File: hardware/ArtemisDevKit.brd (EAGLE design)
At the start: 94 x 38.1 mm, 228 parts, among them J2 CORTEX_JTAG_DEBUG_MINIMUM_PTH, J3 CORTEX_JTAG_DEBUG_PTH, J5 1X04_SMD_STRAIGHT_COMBO, J6 QWIIC_RIGHT_ANGLE, J7 CAMERA-HIMAX, J9 1X04_SMD_STRAIGHT_COMBO, U1 DAPLINK_KL26Z, U2 ARTEMIS_MODULESMD, U3 LIS2DH12, U4 AP2127K-1.8V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

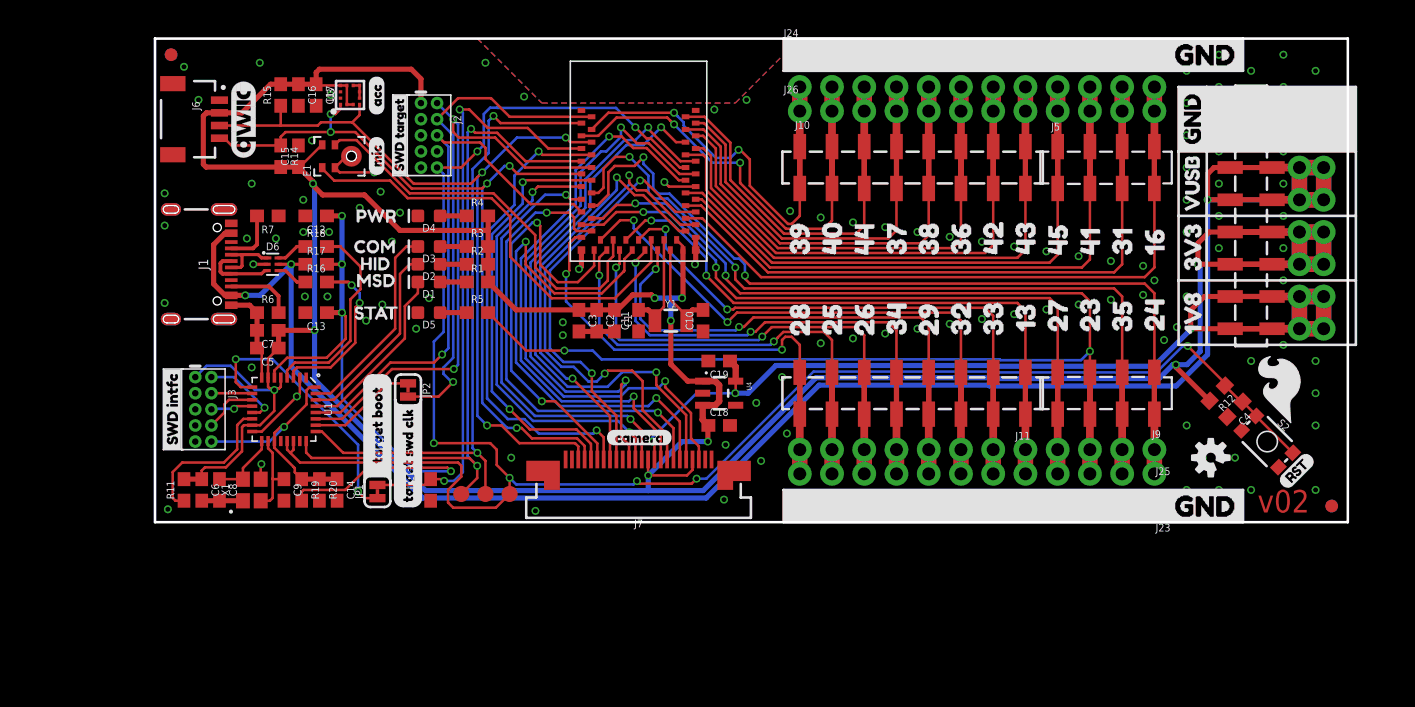
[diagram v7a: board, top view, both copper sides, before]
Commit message: remove old buzzard libraries and delete old silk
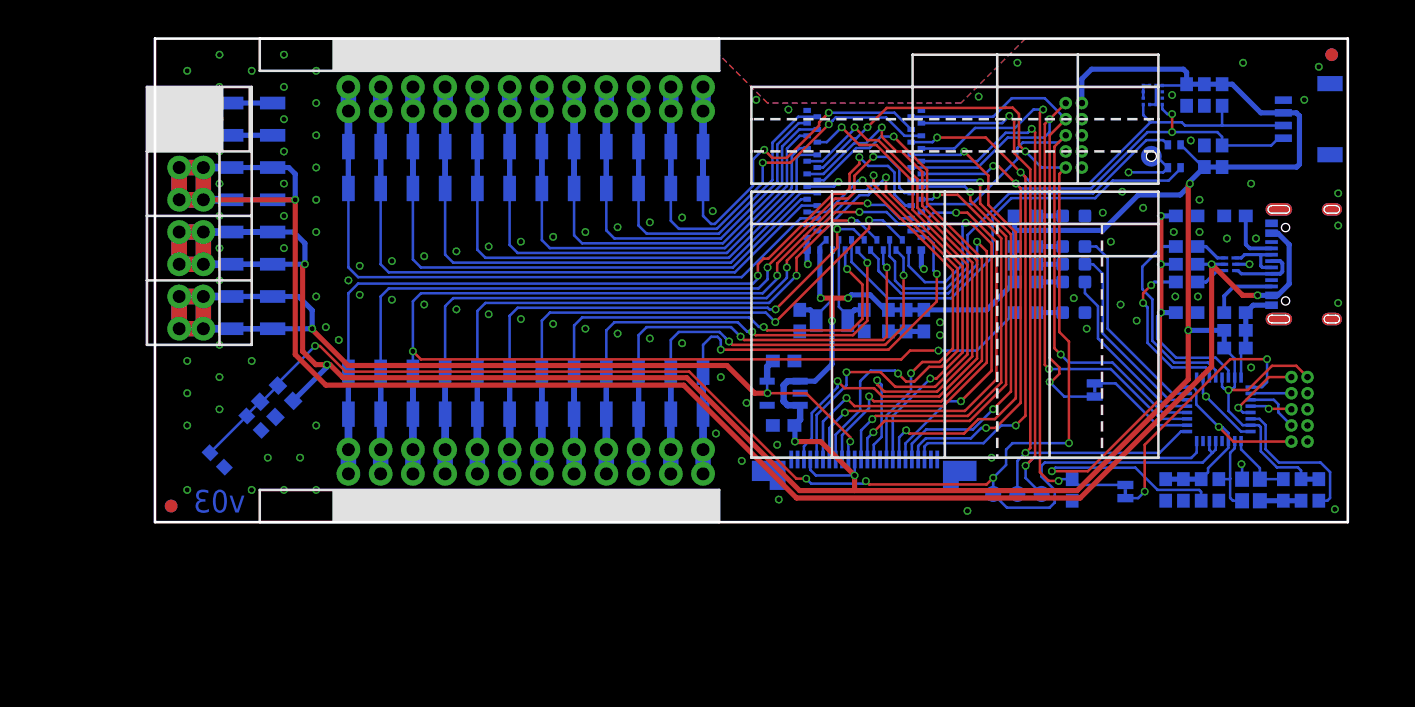
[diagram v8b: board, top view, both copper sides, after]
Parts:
- removed LOGO2: SFE_LOGO_NAME_FLAME.2_INCH, SparkFun-Aesthetics:SFE_LOGO_NAME_FLAME_.2
- removed U$1: (no value), 4mar2020_1:RST6
- removed U$10, U$114, U$145, U$50, U$94: (no value), pin_labels:442
- removed U$100: (no value), info:PWM7
- removed U$101, U$137, U$29, U$69: (no value), pin_labels:2321
- removed U$102, U$140: (no value), info:TX9
- removed U$103, U$132: (no value), info:RX10
- removed U$104: (no value), info:UART18
- removed U$105, U$31, U$71: (no value), pin_labels:2423
- removed U$106, U$122, U$21, U$61, U$98: (no value), pin_labels:2513
- removed U$107, U$138, U$22, U$62: (no value), pin_labels:2614
- removed U$108, U$141, U$28, U$68, U$97: (no value), pin_labels:2720
- removed U$109, U$142, U$20, U$60, U$99: (no value), pin_labels:2812
- removed U$11, U$110, U$124, U$51: (no value), pin_labels:373
- removed U$111, U$126, U$143, U$48, U$8, U$96: (no value), pin_labels:390
- removed U$112, U$128, U$14, U$54, U$93: (no value), pin_labels:426
- removed U$113, U$129, U$15, U$55, U$92: (no value), pin_labels:437
- removed U$115, U$147, U$16, U$56: (no value), pin_labels:458
- removed U$116, U$130, U$27, U$67, U$77: (no value), pin_labels:1319
- removed U$117, U$134, U$24, U$64, U$79: (no value), pin_labels:2916
- removed U$118, U$135, U$18, U$58, U$80: (no value), pin_labels:3110
- removed U$119, U$25, U$65, U$81: (no value), pin_labels:3217
- removed U$12, U$125, U$52, U$91: (no value), pin_labels:384
- removed U$120, U$26, U$66, U$82: (no value), pin_labels:3318
- removed U$121, U$131, U$30, U$70, U$84: (no value), pin_labels:3522
- removed U$123, U$13, U$53: (no value), pin_labels:365
- removed U$127, U$144, U$49, U$9, U$95: (no value), pin_labels:401
- removed U$133, U$19, U$59, U$78: (no value), pin_labels:1611
- removed U$136, U$23, U$63, U$83: (no value), pin_labels:3415
- removed U$139: (no value), info:UART011
- removed U$146, U$17, U$57: (no value), pin_labels:419
- removed U$148, U$149, U$2, U$3: (no value), 4mar2020_1:GND0
- removed U$33: (no value), 4mar2020_1:SWD_TARGET7
- removed U$34: (no value), 4mar2020_1:SWD_INTFC8
- removed U$35: (no value), 4mar2020_1:CAMERA11
- removed U$36: (no value), 4mar2020_1:MIC9
- removed U$37: (no value), 4mar2020_1:ACC10
- removed U$38: (no value), 29may2020_1:TARGET_BOOT0
- removed U$39: (no value), 4mar2020_1:PWR13
- removed U$4: (no value), 4mar2020_1:GND2
- removed U$40: (no value), 4mar2020_1:MSD16
- removed U$41: (no value), 4mar2020_1:HID15
- removed U$42: (no value), 4mar2020_1:COM14
- removed U$43: (no value), 4mar2020_1:STAT17
- removed U$44: (no value), 29may2020_1:TARGET_SWD_CLK1
- removed U$47: (no value), 29may2020_1:ARTEMIS_DEV_KIT2
- removed U$5: (no value), 4mar2020_1:3V34
- removed U$6: (no value), 4mar2020_1:1V85
- removed U$7: (no value), 4mar2020_1:VUSB5
- removed U$72: (no value), 4mar2020_1:GND1
- removed U$73: (no value), 4mar2020_1:1V83
- removed U$74: (no value), 4mar2020_1:3V32
- removed U$75: (no value), 4mar2020_1:VUSB4
- removed U$76: (no value), info:ADC0
- removed U$85: (no value), info:IOM21
- removed U$86: (no value), info:IOM32
- removed U$87: (no value), info:IOM43
- removed U$88: (no value), info:SCL#SCLK4
- removed U$89: (no value), info:SDA#MISO5
- removed U$90: (no value), info:MOSI6
- moved FD1 91.4 mm to (92.7, 36.8), flipped to the bottom
- moved FD2 91.4 mm to (92.7, 36.8), flipped to the top
- moved FD3 91.4 mm to (1.27, 1.27), flipped to the bottom
- moved FD4 91.4 mm to (1.27, 1.27), flipped to the top
- moved J8 90.2 mm to (1.91, 33.0), flipped to the bottom
- moved R11 89.4 mm to (91.7, 2.54), flipped to the bottom
- moved C6 86.6 mm to (90.3, 2.54), flipped to the bottom
- moved J12 86.4 mm to (3.81, 33.0), flipped to the bottom
- moved J3 86.4 mm to (90.2, 8.89), flipped to the bottom
- moved C8 83.8 mm to (88.9, 2.54), flipped to the bottom
- moved J6 83.8 mm to (88.9, 31.8), flipped to the bottom
- moved U$45 83.8 mm to (5.08, 10.8), flipped to the bottom
- moved J1 81.3 mm to (87.6, 20.3), flipped to the bottom
- moved S2 81.3 mm to (6.35, 6.35), flipped to the bottom
- moved U$32 80.0 mm to (87.0, 31.8), flipped to the bottom
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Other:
- board text added: "v03"
- board text removed: "v02"
